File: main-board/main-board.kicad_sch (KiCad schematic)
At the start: 60 parts, among them J1 Conn_02x08_Odd_Even, J2 7-12V, Q1 2N7000, Q2 2N7000, Q3 2N7000, Q4 2N7000, Q5 2N7000, Q6 2N7000, Q7 2N7000, Q8 2N7000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

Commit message: pth layout in progress
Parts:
- removed D3: LED, LED_THT:LED_D3.0mm, symbol Device:LED
- removed Q1, Q2, Q3, Q4, Q5, Q6, Q7, Q8: 2N7000, Package_TO_SOT_THT:TO-92_Inline, symbol Transistor_FET:2N7000
- removed Q9: 2N3904, Package_TO_SOT_THT:TO-92_Inline, symbol Transistor_BJT:2N3904
- removed R10, R4, R5, R7, R8, R9: 360, Resistor_THT:R_Axial_DIN0207_L6.3mm_D2.5mm_P10.16mm_Horizontal, symbol Device:R
- removed TP1, TP2, TP3, TP4, TP5, TP6, TP7, TP8: TestPoint, ezee-footprints:TestPoint_Pad_D1.0mm, symbol Connector:TestPoint
- removed U9: L7805, Package_TO_SOT_THT:TO-220-3_Vertical, symbol Regulator_Linear:L7805
- added Q1, Q2, Q3, Q4, Q5, Q6, Q7, Q8: BC338, Package_TO_SOT_THT:TO-92_Inline, symbol Transistor_BJT:BC338
- added R12, R15, R16, R17, R18: 22k, Resistor_THT:R_Axial_DIN0207_L6.3mm_D2.5mm_P10.16mm_Horizontal, symbol Device:R
- added R22, R23, R24, R25, R26, R27, R28: 180, Resistor_THT:R_Axial_DIN0207_L6.3mm_D2.5mm_P10.16mm_Horizontal, symbol Device:R
- C1: value 0.22u -> 1u
- C2: value 10u -> 4.7u
- J1: now fitted
- J2: footprint ezee-footprints:Battery_Terminals -> kicad-ezee-footprints:Battery_Terminals; now fitted
- R1: value 12k -> 470
- R11, R13, R14: value 360 -> 22k
- R2: value 5.6k -> 4.7k
- R21: renamed from R6; value 360 -> 180
- RV1: value 10k -> 100k; footprint ezee-footprints:Potentiometer_Wheel_3pin_Pitch4mm -> kicad-ezee-footprints:Potentiometer_Wheel_3pin_Pitch4mm
- TP10, TP11: footprint ezee-footprints:TestPoint_Pad_D1.0mm -> kicad-ezee-footprints:TestPoint_Pad_D1.0mm
- TPH1, TPH2: footprint ezee-footprints:TestPoint_Hook -> kicad-ezee-footprints:TestPoint_Hook; symbol ezee-symbols:TestPoint_Hook -> kicad-ezee-symbols:TestPoint_Hook; now in the parts list
- renumbered R12 to R4
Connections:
- net +5V: now also R21.2, R22.2, R23.2, R24.2, R25.2, R26.2, R27.2, R28.2; no longer R13.2, R14.2
- net at J1.13 (Pin_13): now also Q7.3 (E)
- net at J1.5 (Pin_5): now also Q3.3 (E)
- net at U4.13 (D2): now also R13.2
- net at U6.14 (O5): now also J1.10 (Pin_10)
- net at R21.1: now also Q1.1 (C); no longer U6.13 (O6)
- net at J1.12 (Pin_12): now also U6.13 (O6); no longer R21.2
- net at J1.3 (Pin_3): now also Q2.3 (E)
- net at U4.11 (D0): now also R11.2
- net at U4.12 (D1): now also R12.2
- net at U4.15 (D3): now also R14.2
- net at U4.16 (D4): now also R15.2
- net at U4.17 (D5): now also R16.2
- net at U4.18 (D6): now also R17.2
- net at U4.19 (D7): now also R18.2
- net at J1.11 (Pin_11): now also Q6.3 (E)
- net at J1.15 (Pin_15): now also Q8.3 (E)
- net at R14.1: now also Q4.2 (B)
- net at U6.11 (O8): now also J1.16 (Pin_16)
- net at J1.7 (Pin_7): now also Q4.3 (E)
- net at J1.1 (Pin_1): now also Q1.3 (E)
- net at R11.1: now also Q1.2 (B); no longer U6.18 (O1)
- net at J1.2 (Pin_2): now also U6.18 (O1); no longer R11.2
- net at U6.12 (O7): now also J1.14 (Pin_14)
- net at R13.1: now also Q3.2 (B)
- net at U6.15 (O4): now also J1.8 (Pin_8)
- net at U6.16 (O3): now also J1.6 (Pin_6)
- net at J1.9 (Pin_9): now also Q5.3 (E)
- net at J1.4 (Pin_4): now also U6.17 (O2)
- new net: Q2.1 (C), R22.1
- new net: Q2.2 (B), R12.1
- new net: Q4.1 (C), R24.1
- new net: Q7.1 (C), R27.1
- new net: Q7.2 (B), R17.1
- new net: Q8.1 (C), R28.1
- new net: Q8.2 (B), R18.1
- new net: Q3.1 (C), R23.1
- new net: Q5.1 (C), R25.1
- new net: Q6.1 (C), R26.1
- new net: Q5.2 (B), R15.1
- new net: Q6.2 (B), R16.1
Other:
- note added: "f = 1/(470*1E-6) = 2178Hz"
- note added: "fps(min) = 1/( (4.7k+100k) * 4.7E-6) = 2Hz fps(max) = 1/(4.7k * 1E-6) = 48 Hz"
- note removed: "I(led) = 5V-1.7V/360 = 12.6mA"
- note removed: "NOOB!!! - Kan ikke bruke n-channels for high side switchin - GS må være minst 3V, men med Vg=5V så må source være 2V for at fet skal være åpen=>ikke nok til å drive leds - Kan bruke P-channel BS250, men da blir signalet invertert, så alle bytes i eeprom må inverteres. Dessuten er de dyre - Går tilbake til NPN transistorer"
- note removed: "PRØV PÅ BREADBOARD"
- note removed: "TO-220"
- note removed: "Vg=Vled+Vbe = 1.8V+0.6V = 2.4V Ic=20mA Beta=200 Ib=0.02/200 = 0.1mA R=V/I = (5-2.4)/0.1mA ≃ 26000 = 27k resistor"
- note removed: "f = 1/(12000*0.2E-6) = 378Hz"
- note removed: "fps(min) = 1/(15600*10E-6) = 6.4Hz fps(max) = 1/(5600*10E-6) = 18 Hz"
- moved on the sheet: R21

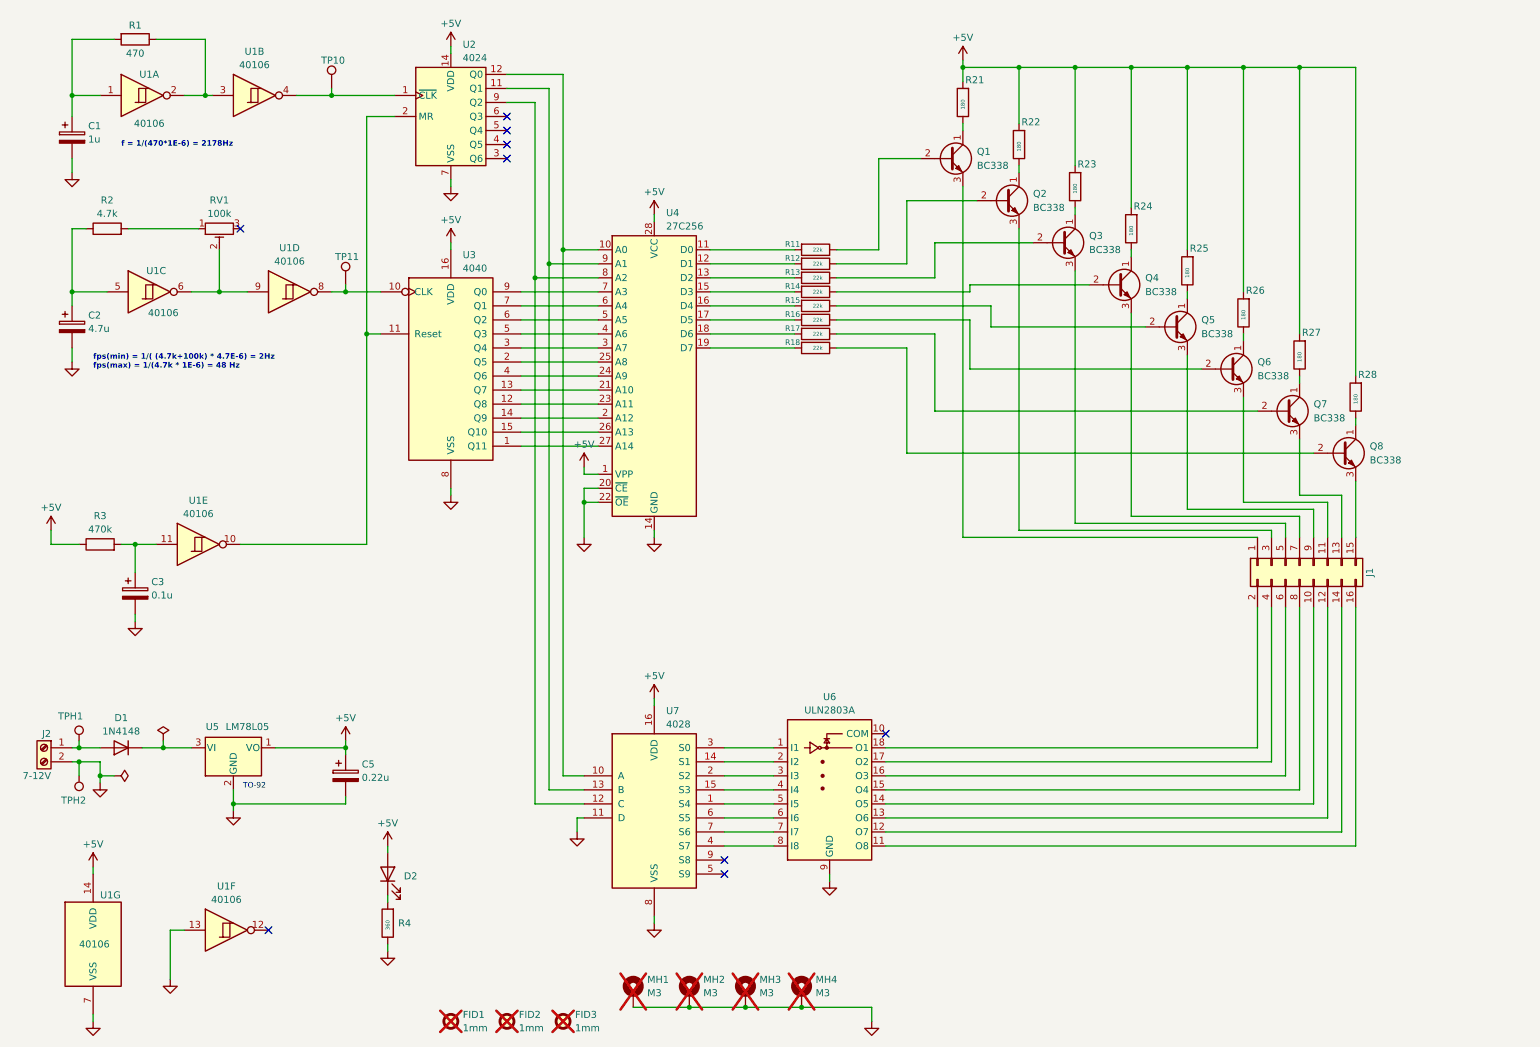
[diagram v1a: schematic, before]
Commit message: completed pth layout for production
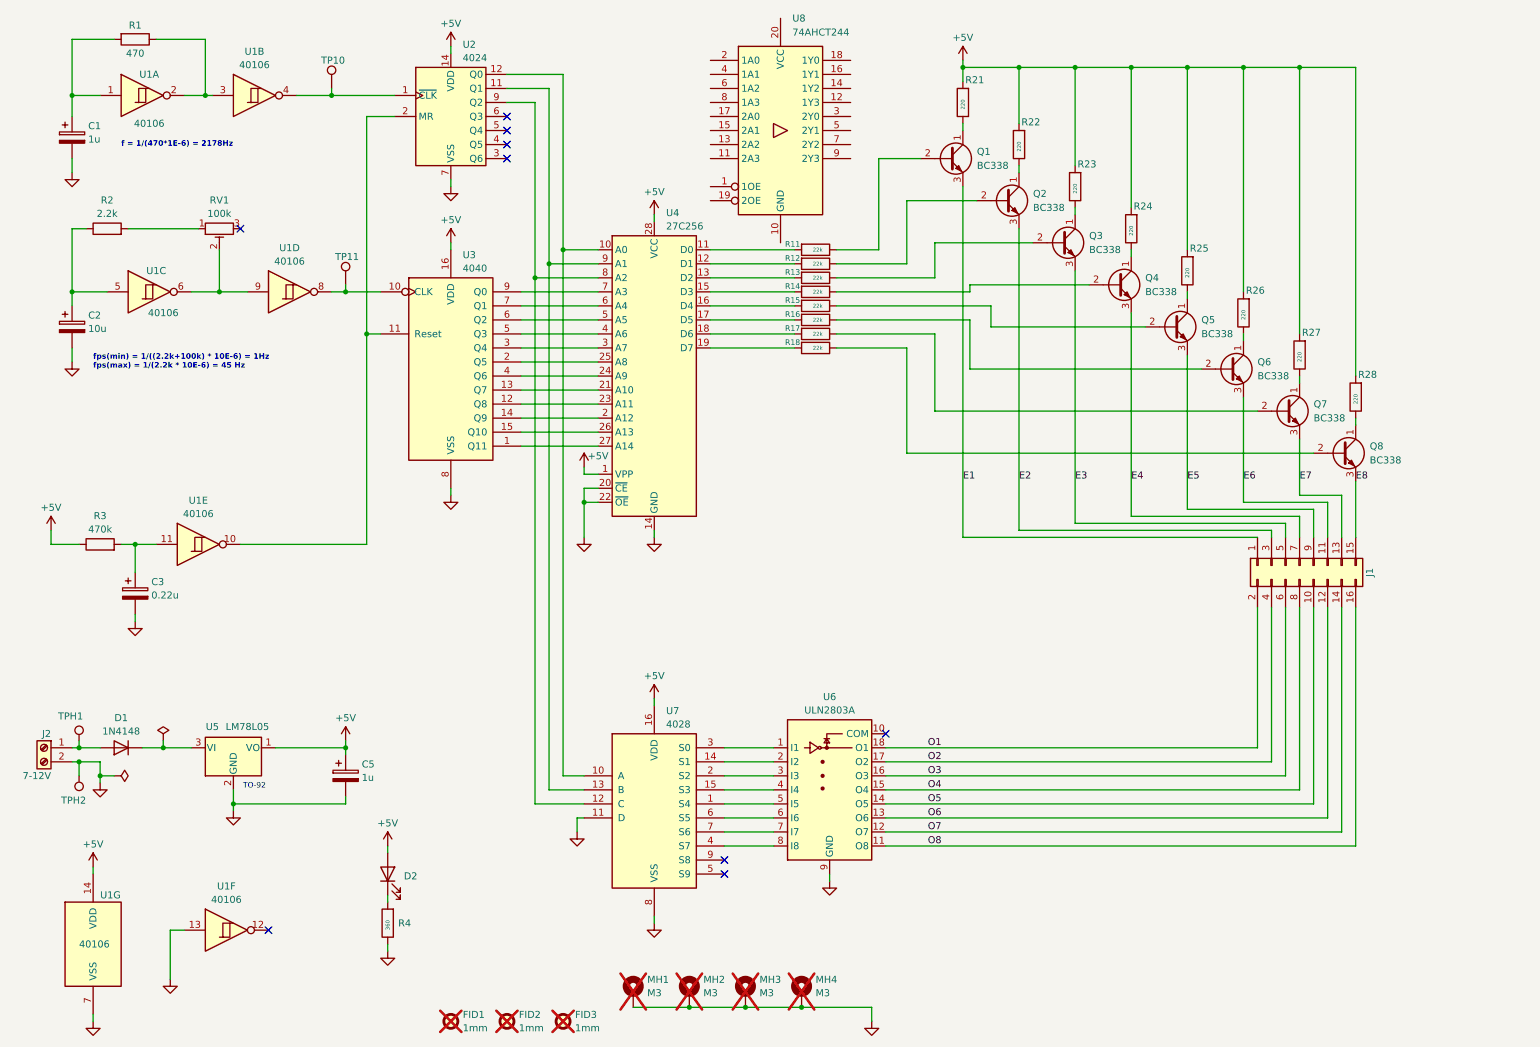
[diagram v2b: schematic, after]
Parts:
- added U8: 74AHCT244, symbol 74xx:74AHCT244
- C2: value 4.7u -> 10u
- C3: value 0.1u -> 0.22u
- C5: value 0.22u -> 1u
- R2: value 4.7k -> 2.2k
- R21, R22, R23, R24, R25, R26, R27, R28: value 180 -> 220
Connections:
- net E2: now reaches J1.3 (Pin_3), Q2.3 (E)
- net E4: now reaches J1.7 (Pin_7), Q4.3 (E)
- net E7: now reaches J1.13 (Pin_13), Q7.3 (E)
- net E8: now reaches J1.15 (Pin_15), Q8.3 (E)
- net E3: now reaches J1.5 (Pin_5), Q3.3 (E)
- net E5: now reaches J1.9 (Pin_9), Q5.3 (E)
- net E6: now reaches J1.11 (Pin_11), Q6.3 (E)
- net E1: now reaches J1.1 (Pin_1), Q1.3 (E)
- net O5: now reaches J1.10 (Pin_10), U6.14 (O5)
- net O6: now reaches J1.12 (Pin_12), U6.13 (O6)
- net O7: now reaches J1.14 (Pin_14), U6.12 (O7)
- net O8: now reaches J1.16 (Pin_16), U6.11 (O8)
- net O1: now reaches J1.2 (Pin_2), U6.18 (O1)
- net O2: now reaches J1.4 (Pin_4), U6.17 (O2)
- net O3: now reaches J1.6 (Pin_6), U6.16 (O3)
- net O4: now reaches J1.8 (Pin_8), U6.15 (O4)
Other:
- note added: "fps(min) = 1/((2.2k+100k) * 10E-6) = 1Hz fps(max) = 1/(2.2k * 10E-6) = 45 Hz"
- note removed: "fps(min) = 1/( (4.7k+100k) * 4.7E-6) = 2Hz fps(max) = 1/(4.7k * 1E-6) = 48 Hz"
